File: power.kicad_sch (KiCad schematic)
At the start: 49 parts, among them J1 PWR + CAN harness, Q1 100V 4.3mOhm N-ch, U1 LM74700-Q1, U2 LM5164-Q1 (5V), U3 LM5164-Q1 (3V3)

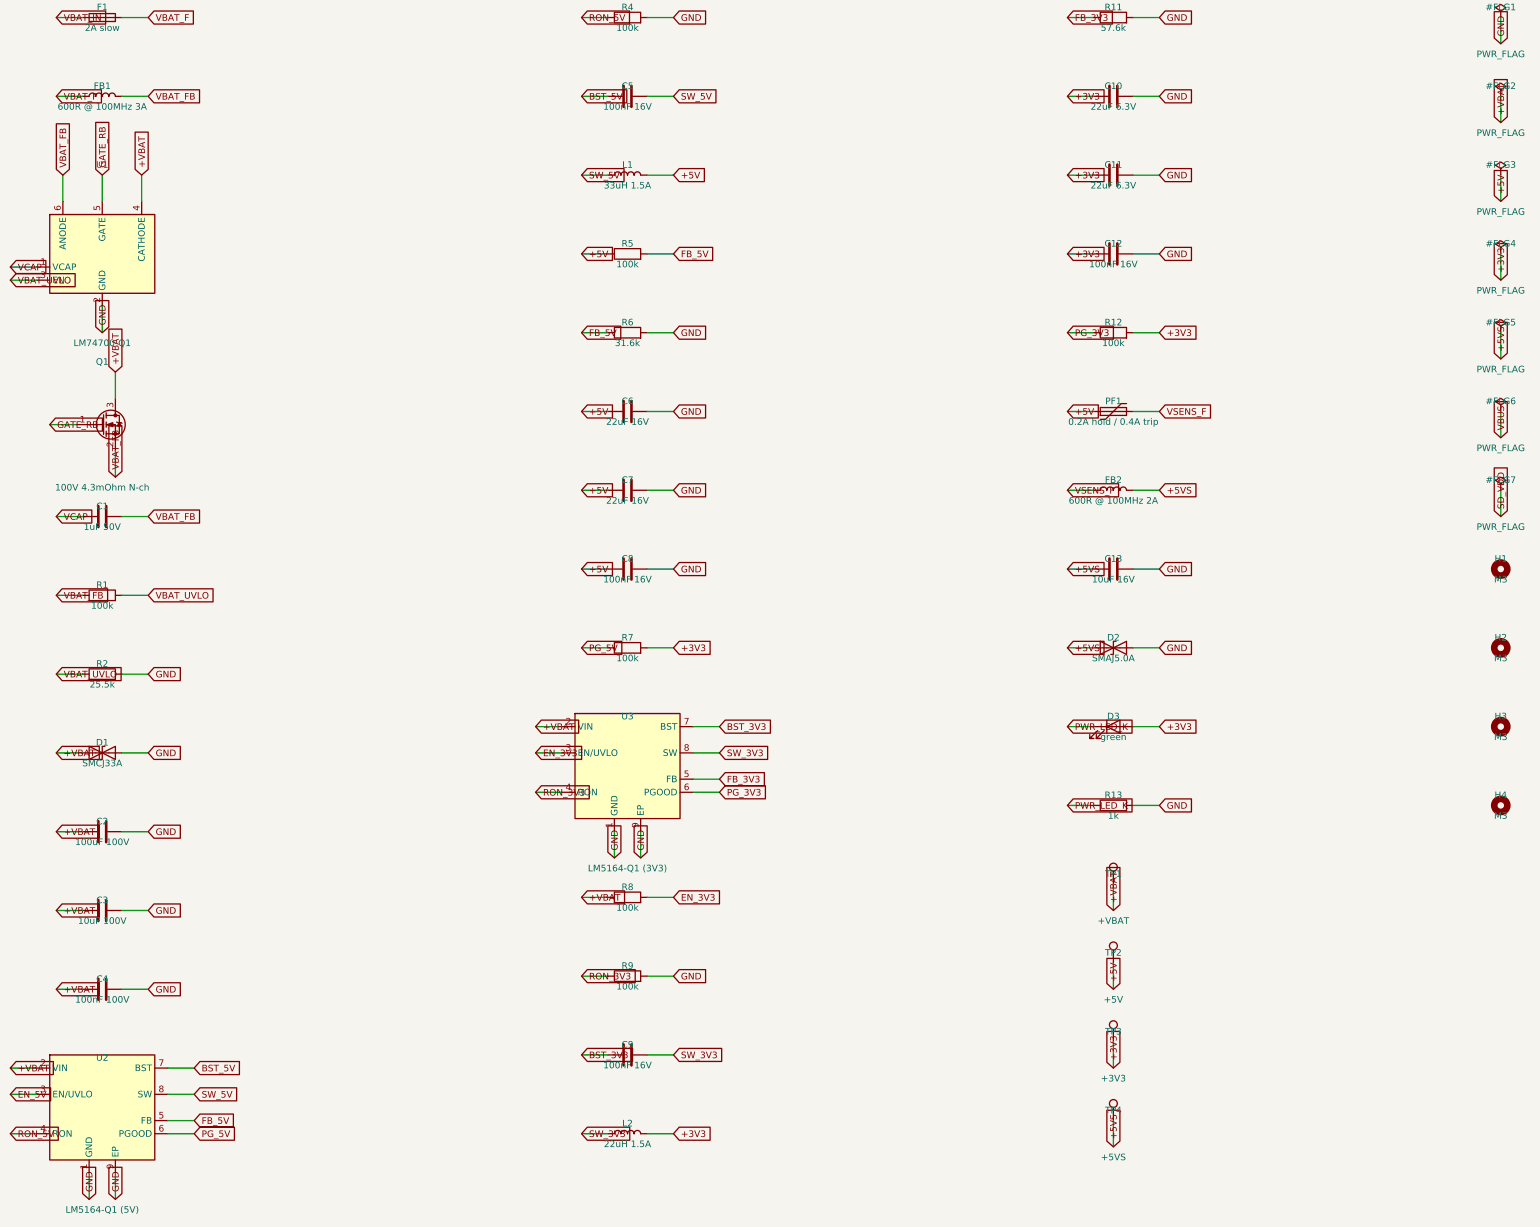
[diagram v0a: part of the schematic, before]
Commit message: Pass ERC clean on KiCad 9.0 and regenerate against its libraries
- Add a PWR_FLAG on VBAT_FB so the LM74700 ANODE power-input pin, fed
  through the reverse-battery FET and EMI bead, no longer trips
  power_pin_not_driven.
- Resolve the generic MOSFET symbols from Transistor_FET where the
  KiCad 9 libraries moved them out of Device.
- Handle the KiCad 9 library format in the raw-symbol extractor: tab
  indentation, CRLF line endings, and no trailing space after the
  symbol name.
- Flatten derived symbols the way KiCad does — carry the child's whole
  property blocks into the parent geometry instead of only swapping the
  value strings — so the embedded USBLC6-2SC6 matches the library copy.
- Regenerate all sheets, netlist, and the PDF plot; embedded symbol
  definitions now come from the KiCad 9.0 (20241209) libraries.

Validated with kicad-cli 9.0: all sheets load, connectivity matches
netlist.txt on 102 nets / 153 instances, ERC clean.

Co-Authored-By: Claude Fable 5 <noreply@anthropic.com>
Claude-Session: https://claude.ai/code/session_01DhNbL25h25p8VFCjRfJik9
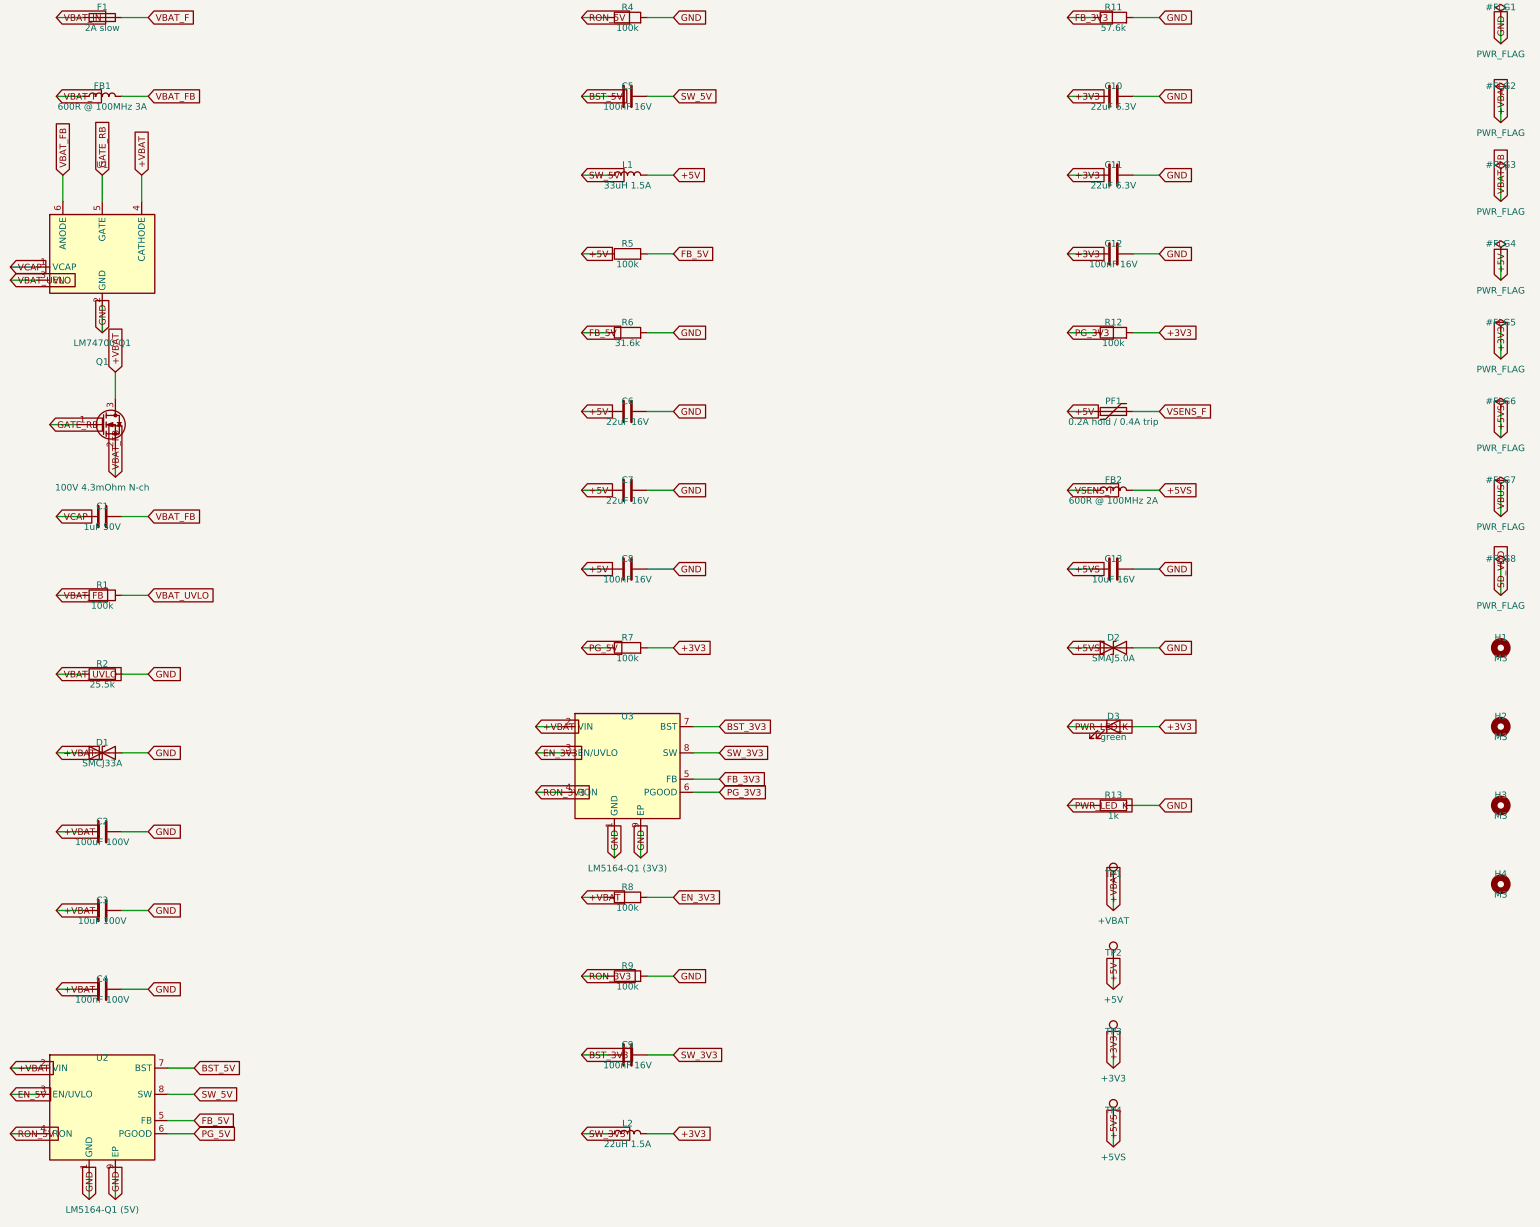
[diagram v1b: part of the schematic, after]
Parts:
- Q1: symbol Device:Q_NMOS_GSD -> Transistor_FET:Q_NMOS_GSD
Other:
- moved on the sheet: H1, H2, H3, H4

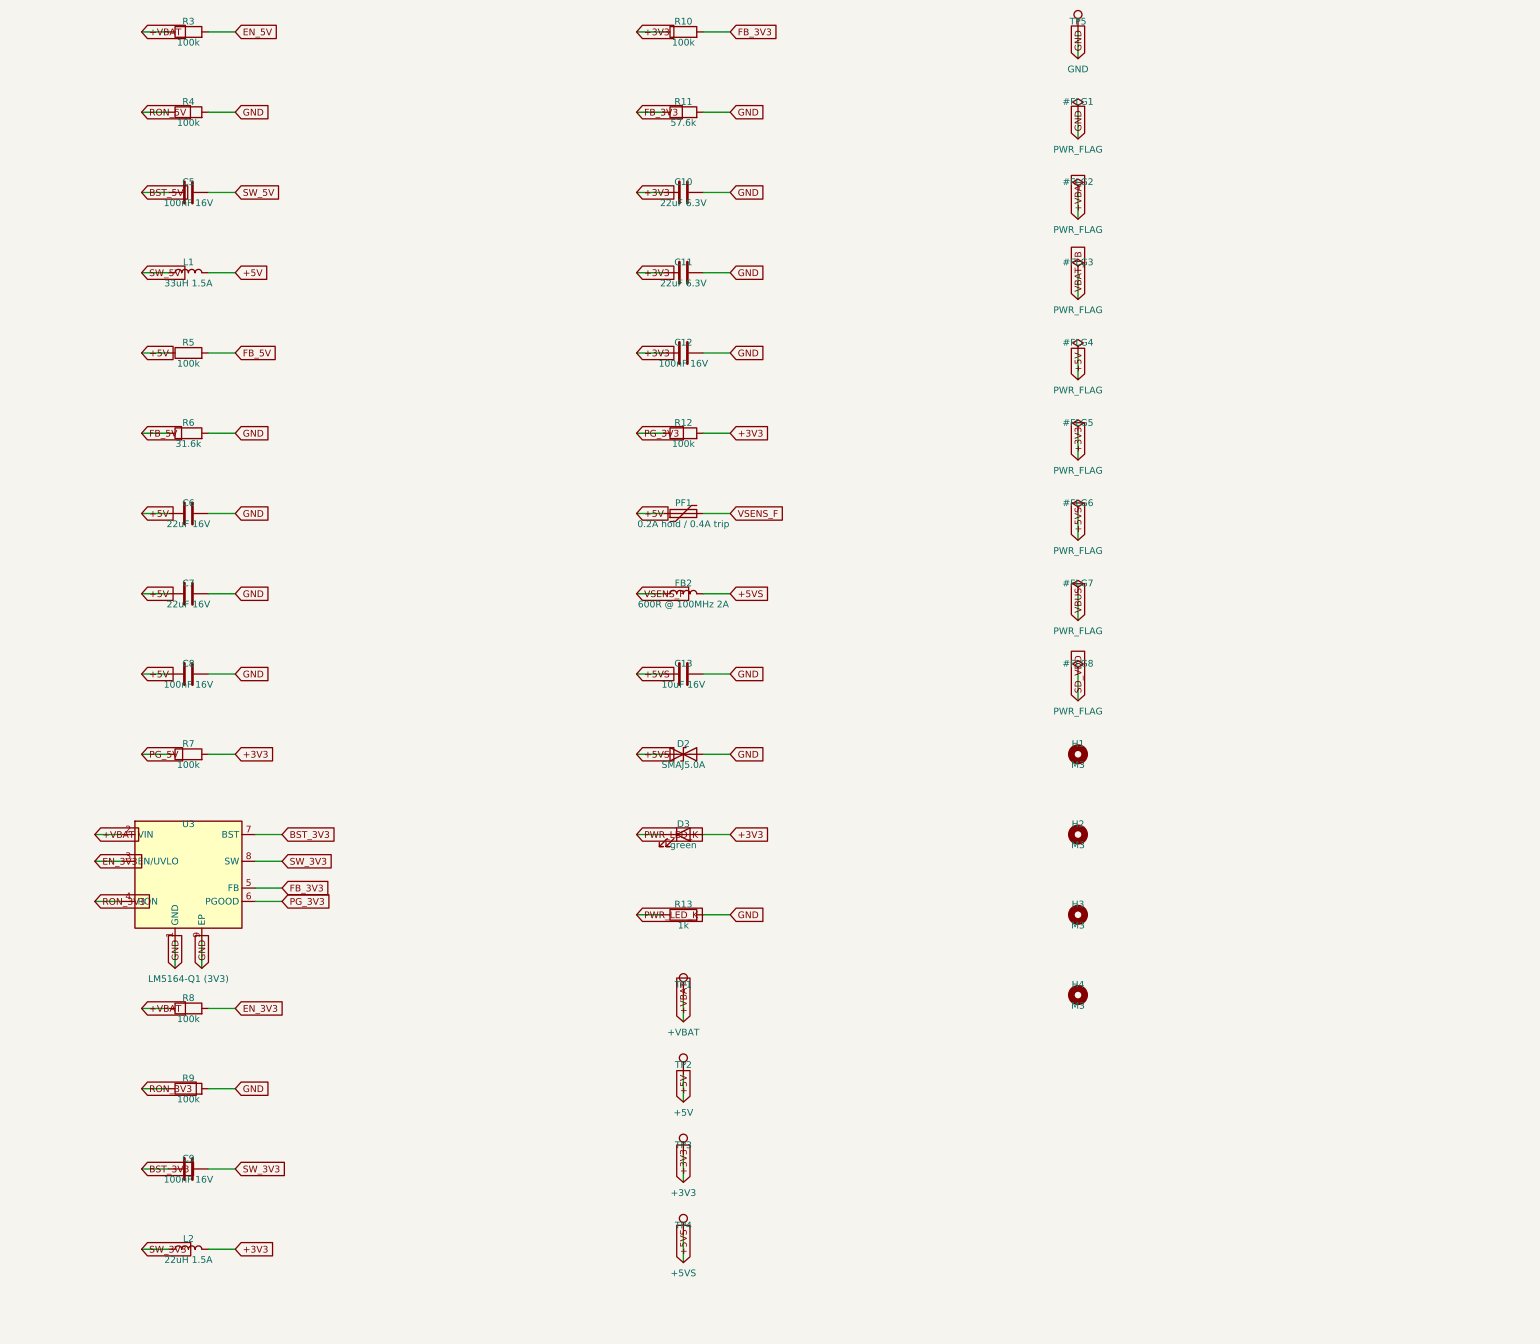
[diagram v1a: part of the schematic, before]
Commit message: Fix the LM5164 power stages against the datasheet and TI's DDA drawing
Review of datasheet SNVSAU4D and package drawing 4214849/B (DDA0008B)
caught five issues, all fixed and re-verified:

- RON placeholders (100k -> ~125/83kHz) corrected to 31.6k (396kHz, 5V)
  and 20.5k (402kHz, 3V3); minimum on-time at the 53.3V clamp is
  237ns/154ns, well above the 50ns floor.
- Bootstrap caps were 100nF; the datasheet mandates exactly 2.2nF and
  warns larger values damage the internal VCC regulator. Now 2.2nF 50V.
- No FB ripple injection on the all-ceramic outputs -- a COT stability
  requirement (Table 6-1). Added Type-3 networks (RA/CA/CB: 121k and
  95.3k / 3.3nF / 270pF) sized for ~20mV ramp at 14V per TI's example.
- Exposed-pad footprint EP2.41x3.3mm was smaller than the DDA0008B pad
  itself (max 2.71x3.4mm); swapped to the EP2.95x4.9mm_Mask2.71x3.4mm
  footprint matching TI's example land pattern.
- Quantified BAT54S back-feed into +3V3: one input shorted to battery
  floats the rail to ~3.6V when the MCU sleeps. Added D2, an MM3Z3V6T1G
  3.6V zener rail clamp.

Load-dump assumption confirmed by the owner: alternator never exceeds
20V, so the SMCJ33A standoff has comfortable margin.

Validated with kicad-cli 9.0: 104 nets / 160 instances match, ERC clean.

Co-Authored-By: Claude Fable 5 <noreply@anthropic.com>
Claude-Session: https://claude.ai/code/session_01DhNbL25h25p8VFCjRfJik9
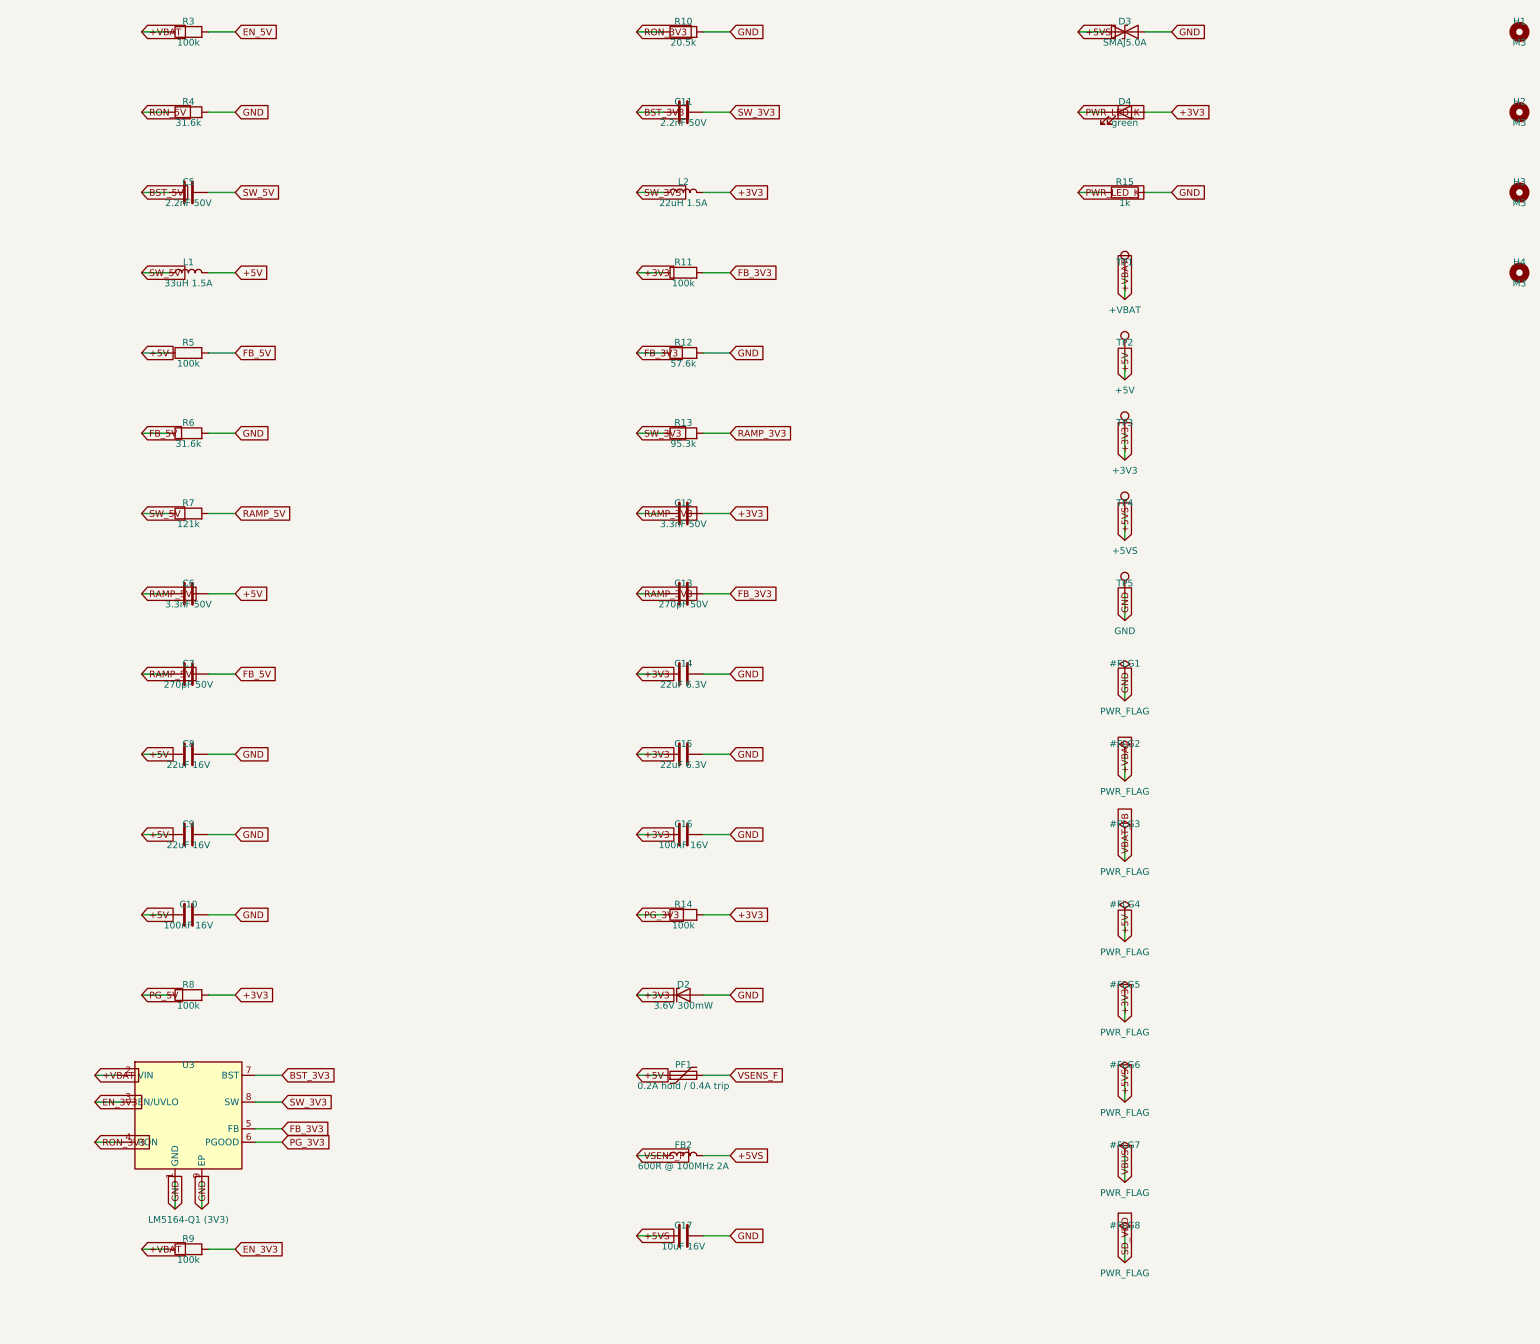
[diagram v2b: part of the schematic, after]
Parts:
- added C14, C15: 22uF 6.3V, Capacitor_SMD:C_1206_3216Metric, symbol Device:C
- added C16: 100nF 16V, Capacitor_SMD:C_0805_2012Metric, symbol Device:C
- added C17: 10uF 16V, Capacitor_SMD:C_1206_3216Metric, symbol Device:C
- added D4: green, LED_SMD:LED_0805_2012Metric, symbol Device:LED
- added R14: 100k, Resistor_SMD:R_0805_2012Metric, symbol Device:R
- added R15: 1k, Resistor_SMD:R_0805_2012Metric, symbol Device:R
- C10: value 22uF 6.3V -> 100nF 16V; footprint Capacitor_SMD:C_1206_3216Metric -> Capacitor_SMD:C_0805_2012Metric
- C11: value 22uF 6.3V -> 2.2nF 50V; footprint Capacitor_SMD:C_1206_3216Metric -> Capacitor_SMD:C_0805_2012Metric; Note (none) -> Bootstrap: datasheet-mandated 2.2nF X7R, do not increase
- C12: value 100nF 16V -> 3.3nF 50V; Note (none) -> Ramp capacitor CA
- C13: value 10uF 16V -> 270pF 50V; footprint Capacitor_SMD:C_1206_3216Metric -> Capacitor_SMD:C_0805_2012Metric; Note (none) -> Ramp coupling capacitor CB
- C5: value 100nF 16V -> 2.2nF 50V; Note Bootstrap -> Bootstrap: datasheet mandates exactly 2.2nF X7R -- a larger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
- C6: value 22uF 16V -> 3.3nF 50V; footprint Capacitor_SMD:C_1206_3216Metric -> Capacitor_SMD:C_0805_2012Metric; Note (none) -> Ramp capacitor CA
- C7: value 22uF 16V -> 270pF 50V; footprint Capacitor_SMD:C_1206_3216Metric -> Capacitor_SMD:C_0805_2012Metric; Note (none) -> Ramp coupling capacitor CB
- C8, C9: value 100nF 16V -> 22uF 16V; footprint Capacitor_SMD:C_0805_2012Metric -> Capacitor_SMD:C_1206_3216Metric
- D2: value SMAJ5.0A -> 3.6V 300mW; footprint Diode_SMD:D_SMA -> Diode_SMD:D_SOD-323; symbol Device:D_TVS -> Device:D_Zener; MPN Littelfuse SMAJ5.0A -> onsemi MM3Z3V6T1G; Note Clamps harness-injected transients on the sensor 5V -> Rail clamp: an analog input shorted to battery back-feeds ~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
- D3: value green -> SMAJ5.0A; footprint LED_SMD:LED_0805_2012Metric -> Diode_SMD:D_SMA; symbol Device:LED -> Device:D_TVS; MPN (none) -> Littelfuse SMAJ5.0A; Note Power indicator -> Clamps harness-injected transients on the sensor 5V
- R10: value 100k -> 20.5k; Note FB upper: 1.2V ref -> 3.28V -> RON = 3.3V x 2500 / 400kHz (Eq 12) -> 402kHz; tON = 154ns a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
- R11: value 57.6k -> 100k; Note FB lower -> FB upper: 1.2V ref -> 3.28V
- R12: value 100k -> 57.6k; Note (none) -> FB lower
- R13: value 1k -> 95.3k; Note (none) -> Ripple-injection ramp resistor RA
- R4: value 100k -> 31.6k; Note On-time set: target ~400kHz at 14V in -- trim per datasheet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 -> RON = 5.0V x 2500 / 400kHz (Eq 12) -> 396kHz; tON = 237ns a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
- R7: value 100k -> 121k; Note Power-good pull-up -> Ripple-injection ramp resistor RA
- R8: Note (none) -> Power-good pull-up
- R9: Note On-time set: target ~400kHz at 14V in -> (none)
- U2, U3: footprint Package_SO:SOIC-8-1EP_3.9x4.9mm_P1.27mm_EP2.41x3.3mm_ThermalVias -> Package_SO:SOIC-8-1EP_3.9x4.9mm_P1.27mm_EP2.95x4.9mm_Mask2.71x3.4mm_ThermalVias
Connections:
- net +3V3: now also C12.2, D2.1 (K), R11.1, R8.2, C14.1, C15.1, C16.1, D4.2 (A), R14.2; no longer C10.1, C11.1, C12.1, D3.2 (A), R10.1, R12.2, R7.2
- net +5V: now also C10.1, C6.2, C9.1; no longer C6.1, C7.1
- net +5VS: now also D3.1 (A1), C17.1; no longer C13.1, D2.1 (A1)
- net +VBAT: now also R9.1; no longer R8.1
- net BST_3V3: now also C11.1; no longer C9.1
- net EN_3V3: now also R9.2; no longer R8.2
- net FB_3V3: now also C13.2, R11.2, R12.1; no longer R10.2, R11.1
- net FB_5V: now also C7.2
- net GND: now also C9.2, D3.2 (A2), R10.2, R12.2, C14.2, C15.2, C16.2, C17.2, R15.2; no longer C11.2, C12.2, C13.2, C6.2, C7.2, R11.2, R13.2, R9.2
- net PG_3V3: now also R14.1; no longer R12.1
- net PG_5V: now also R8.1; no longer R7.1
- net PWR_LED_K: now also D4.1 (K), R15.1; no longer D3.1 (K), R13.1
- net RON_3V3: now also R10.1; no longer R9.1
- net SW_3V3: now also C11.2, R13.1; no longer C9.2
- net SW_5V: now also R7.1
- new net RAMP_3V3: C12.1, C13.1, R13.2
- new net RAMP_5V: C6.1, C7.1, R7.2
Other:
- moved on the sheet: C10, C11, C12, C13, C6, C7, C8, C9, D2, FB2, H1, H2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
